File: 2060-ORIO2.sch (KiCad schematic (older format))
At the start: 185 parts, among them J11 RaspberryPI-B+header, J12 Conn_01x04, J13 Conn_01x08, J14 Conn_01x08, J15 Conn_01x08, J16 Conn_01x10, J17 Conn_01x10, J18 Conn_01x10, J19 Conn_01x10, J20 Conn_01x09, J21 Conn_01x08, J22 Conn_01x08, J23 Conn_01x08, J24 Conn_01x08, J25 Conn_01x08, J26 Conn_01x08, J27 Conn_01x02, J28 Conn_01x16, J29 Conn_01x16, J30 Conn_01x16, J31 Conn_01x08, J32 Conn_01x08, J33 Conn_01x08, J34 Conn_01x08, J35 TBL001-500-02GY-2GY, Q11 ULN2803ADWR, SW11 SW_DIP_x08, U11 ICE40HX4K-TQ144, U12 SN74LVC4245AN, U13 SN74LVC4245AN, U14 SN74LVC4245AN, U15 TPS563231, U16 MCP3008, U17 AZ1117CH-3.3TRG1, U18 AZ1117CH-3.3TRG1, U19 AZ1117CH-1.2, U20 TPS563231, U21 SN74LVC4245AN, U22 SN74LVC4245AN, U23 SN74LVC4245AN, U24 SN74LVC4245AN, U25 TPS563231, U26 AP3012, Y11 XLH536025_000000I

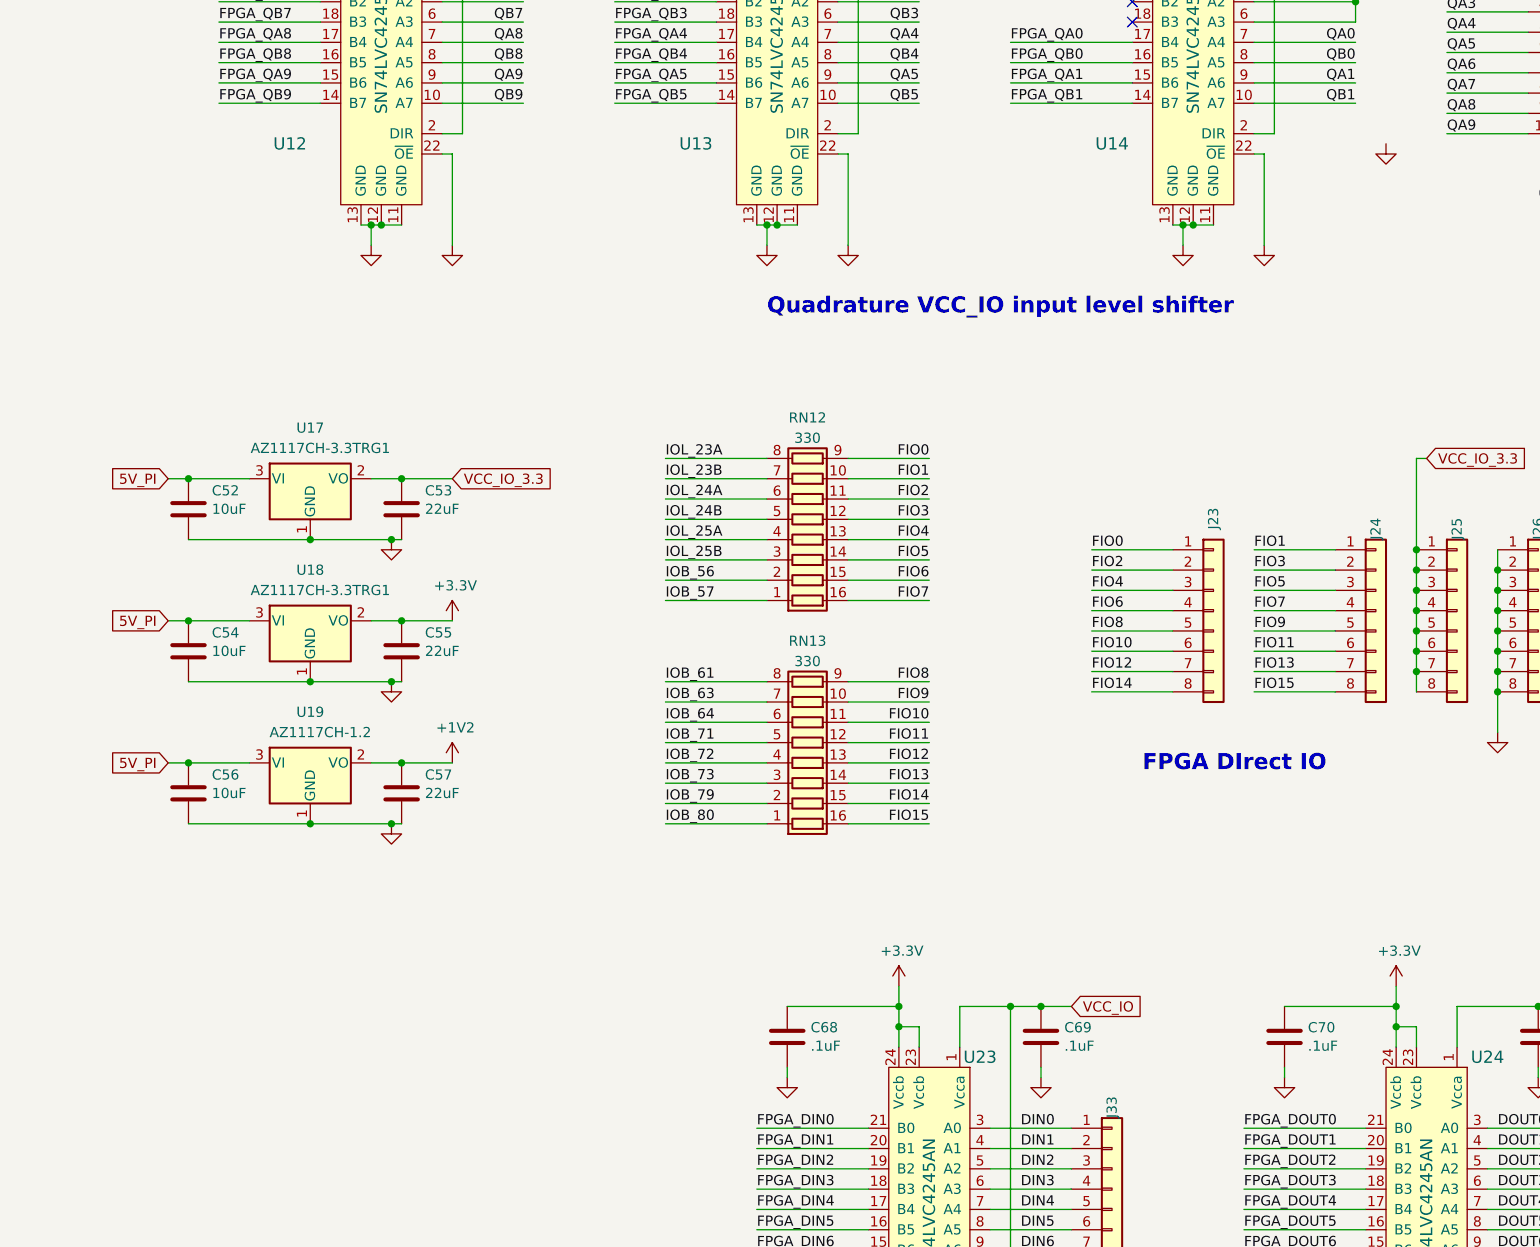
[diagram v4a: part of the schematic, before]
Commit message: Added power LED & GND plane vias.
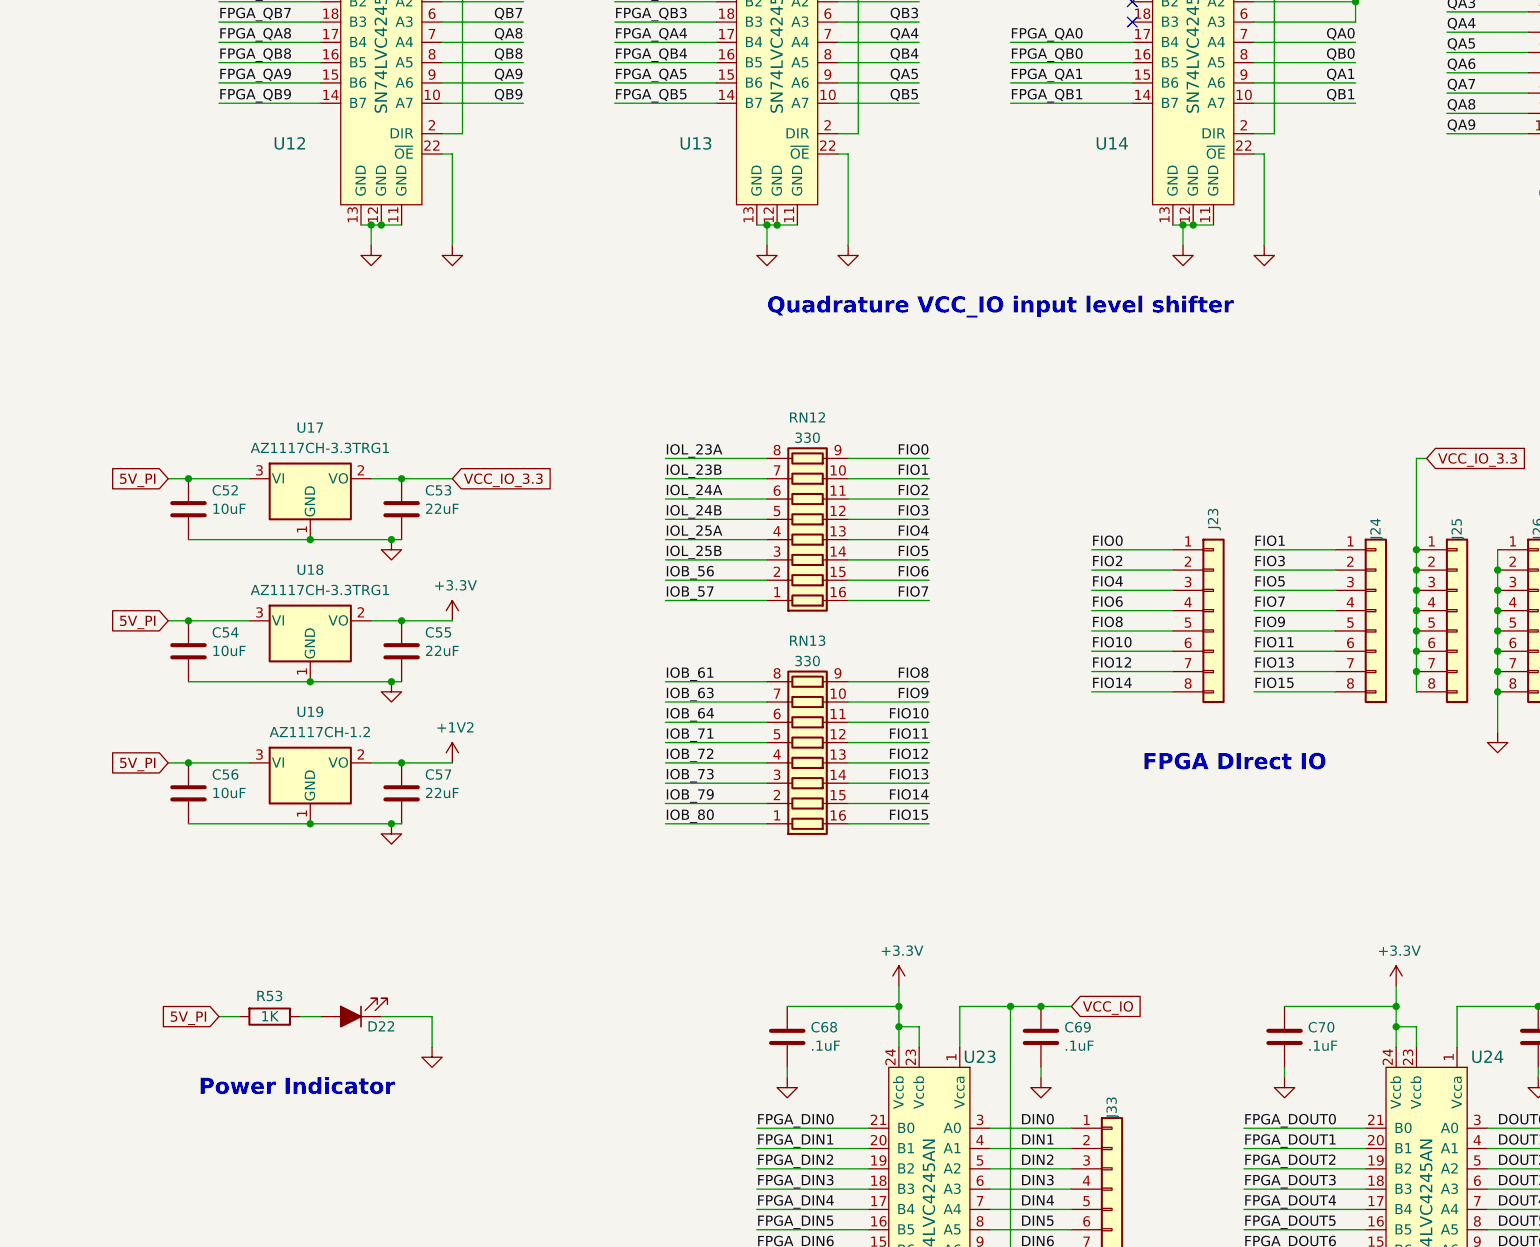
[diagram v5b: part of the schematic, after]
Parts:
- added D22: LED_ALT, LED_SMD:LED_0805_2012Metric_Pad1.15x1.40mm_HandSolder, symbol Device:LED_ALT
- added R53: 1K, Resistor_SMD:R_0603_1608Metric_Pad1.05x0.95mm_HandSolder, symbol Device:R
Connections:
- net 5V_PI: now also R53.2
- net GND: now also D22.1 (K)
- new net: D22.2 (A), R53.1
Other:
- note added: "Power Indicator"
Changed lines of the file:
@@
 	11950 7600 12450 7600
-$Comp
-L power:GND #PWR0121
-U 1 1 5F55C3BD
-P 12600 8200
-F 0 "#PWR0121" H 12600 7950 50  0001 C CNN
-F 1 "GND" H 12605 8027 50  0001 C CNN
-F 2 "" H 12600 8200 50  0001 C CNN
-F 3 "" H 12600 8200 50  0001 C CNN
-	1    12600 8200
-	1    0    0    -1
-$EndComp
 $Comp
 L Device:Net-Tie_2 NT1
@@
 Wire Wire Line
 	12650 7200 12650 7300
+$Comp
+L Device:LED_ALT D22
+U 1 1 5FB53195
+P 7500 12500
+F 0 "D22" H 7350 12550 50  0000 C CNN
+F 1 "LED_ALT" H 7493 12626 50  0001 C CNN
+F 2 "LED_SMD:LED_0805_2012Metric_Pad1.15x1.40mm_HandSolder" H 7500 12500 50  0001 C CNN
+F 3 "~" H 7500 12500 50  0001 C CNN
+F 4 "LED GREEN DIFFUSED 0805 SMD" H 7500 12500 50  0001 C CNN "Description"
+F 5 "475-1410-1-ND" H 7500 12500 50  0001 C CNN "Digi-Key_PN"
+F 6 "LG R971-KN-1" H 7500 12500 50  0001 C CNN "MPN"
+F 7 "OSRAM Opto Semiconductors Inc." H 7500 12500 50  0001 C CNN "Manufacturer"
+	1    7500 12500
+	-1   0    0    1
+$EndComp
+Text GLabel 6850 12500 0    50   Input ~ 0
+5V_PI
+$Comp
+L Device:R R?
+U 1 1 5FB72B9D
+P 7100 12500
+AR Path="/5BBE5CCD/5FB72B9D" Ref="R?"  Part="1"
+AR Path="/5FB72B9D" Ref="R53"  Part="1"
+AR Path="/5CF9559A/5FB72B9D" Ref="R?"  Part="1"
+AR Path="/5ECC13DB/5FB72B9D" Ref="R?"  Part="1"
+F 0 "R53" V 7000 12500 50  0000 C CNN
+F 1 "1K" V 7100 12500 50  0000 C CNN
+F 2 "Resistor_SMD:R_0603_1608Metric_Pad1.05x0.95mm_HandSolder" V 7030 12500 50  0001 C CNN
+F 3 "~" H 7100 12500 50  0001 C CNN
+F 4 "" H 7100 12500 50  0001 C CNN "Digi-Key_PN"
+F 5 "" H 7100 12500 50  0001 C CNN "Description"
+F 6 "" H 7100 12500 50  0001 C CNN "MPN"
+F 7 "Yageo" H 7100 12500 50  0001 C CNN "Manufacturer"
+	1    7100 12500
+	0    1    1    0
+$EndComp
+Wire Wire Line
+	6850 12500 6950 12500
+Wire Wire Line
+	7250 12500 7350 12500
+Wire Wire Line
+	7650 12500 7900 12500
+Wire Wire Line
+	7900 12500 7900 12650
+$Comp
+L power:GND #PWR?
+U 1 1 5FF6D867
+P 7900 12650
+AR Path="/5D1A4D20/5FF6D867" Ref="#PWR?"  Part="1"
+AR Path="/5FF6D867" Ref="#PWR0121"  Part="1"
+AR Path="/5CF9559A/5FF6D867" Ref="#PWR?"  Part="1"
+AR Path="/5E2D04E3/5FF6D867" Ref="#PWR?"  Part="1"
+AR Path="/5F66828B/5FF6D867" Ref="#PWR?"  Part="1"
+F 0 "#PWR0121" H 7900 12400 50  0001 C CNN
+F 1 "GND" H 7905 12477 50  0001 C CNN
+F 2 "" H 7900 12650 50  0001 C CNN
+F 3 "" H 7900 12650 50  0001 C CNN
+	1    7900 12650
+	1    0    0    -1
+$EndComp
+Text Notes 6750 12900 0    79   ~ 16
+Power Indicator
 $EndSCHEMATC

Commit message: Fuses, 4-layer, RSL, 86 the Solenoid GND,
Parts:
- removed J14: Conn_01x08, Connector_PinHeader_2.54mm:PinHeader_1x08_P2.54mm_Vertical, symbol Connector_Generic:Conn_01x08
- added F11: .5A, Fuse:Fuse_2920_7451Metric_Pad2.10x5.45mm_HandSolder, symbol Device:Polyfuse
- added F12: Polyfuse, Fuse:Fuse_2920_7451Metric_Pad2.10x5.45mm_HandSolder, symbol Device:Polyfuse
- added J14: Conn_01x02, Connector_PinHeader_2.54mm:PinHeader_1x02_P2.54mm_Vertical, symbol Connector_Generic:Conn_01x02
- added Q12: BCV27, Package_TO_SOT_SMD:SOT-23, symbol Device:Q_NPN_Darlington_BEC
- added R54: 1K, Resistor_SMD:R_0603_1608Metric_Pad1.05x0.95mm_HandSolder, symbol Device:R
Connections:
- net +BATT: now also F11.2, F12.1; no longer C78.1, D21.1 (K), L14.1, U26.4 (~SHDN), U26.5 (VIN)
- net GND: now also Q12.2 (E)
- net FPGA_RSL: now reaches U11.128 (IOT_197_GBIN1)
- net FPGA_RSL: now also R54.2
- net VCC_SOL renamed VCC_SOL_24
- new net: Q12.1 (B), R54.1
- new net: J14.2 (Pin_2), Q12.3 (C)
- new net: D21.1 (K), F12.2
- new net VCC_SOL_12: C78.1, F11.1, J14.1 (Pin_1), L14.1, U26.4 (~SHDN), U26.5 (VIN)
- no-connect marks 34 -> 33
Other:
- note added: "RSL Light Driver"
- moved on the sheet: C78, C79, D20, J13, L14, R51, R52, U26

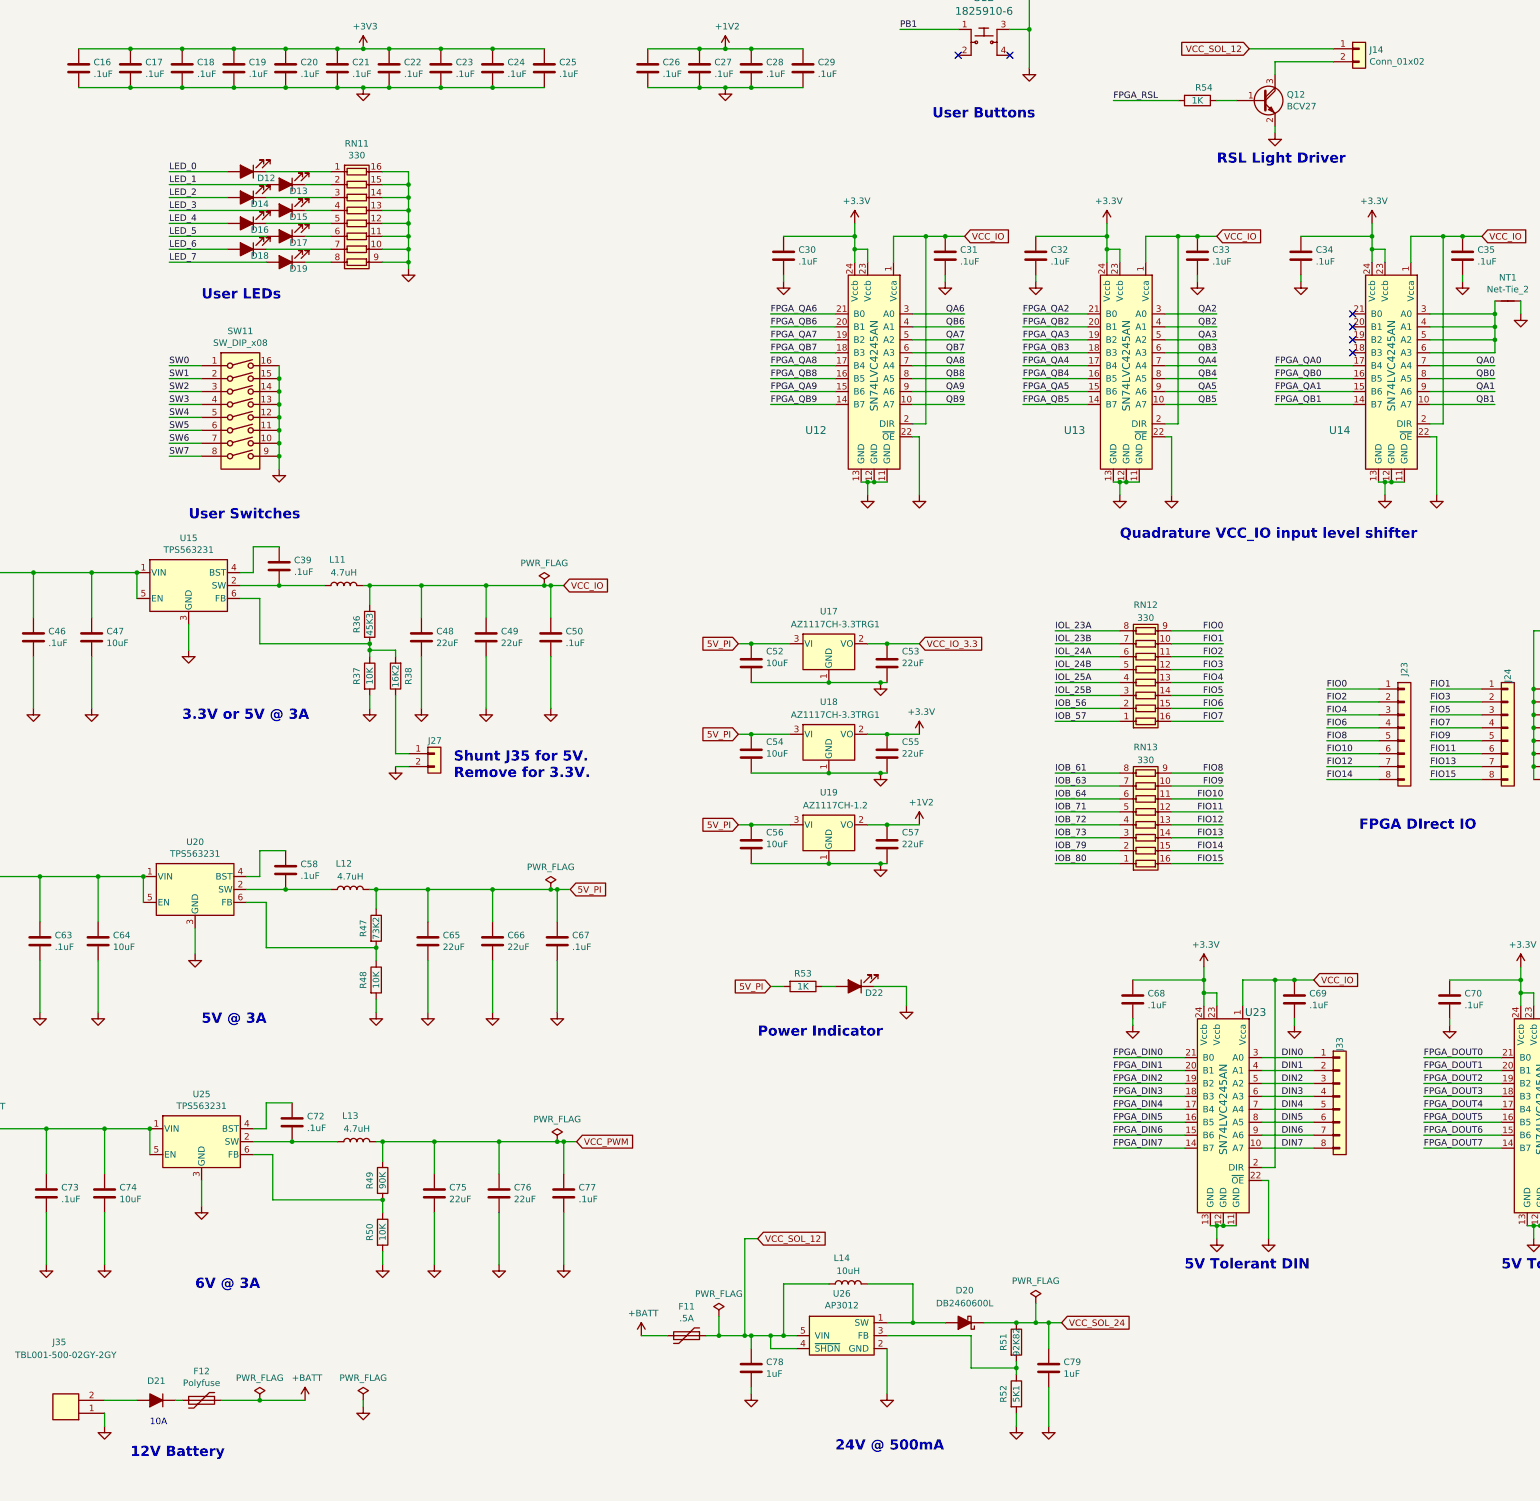
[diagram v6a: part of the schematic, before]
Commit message: Added pul;lup resistors on DIN level shifters.
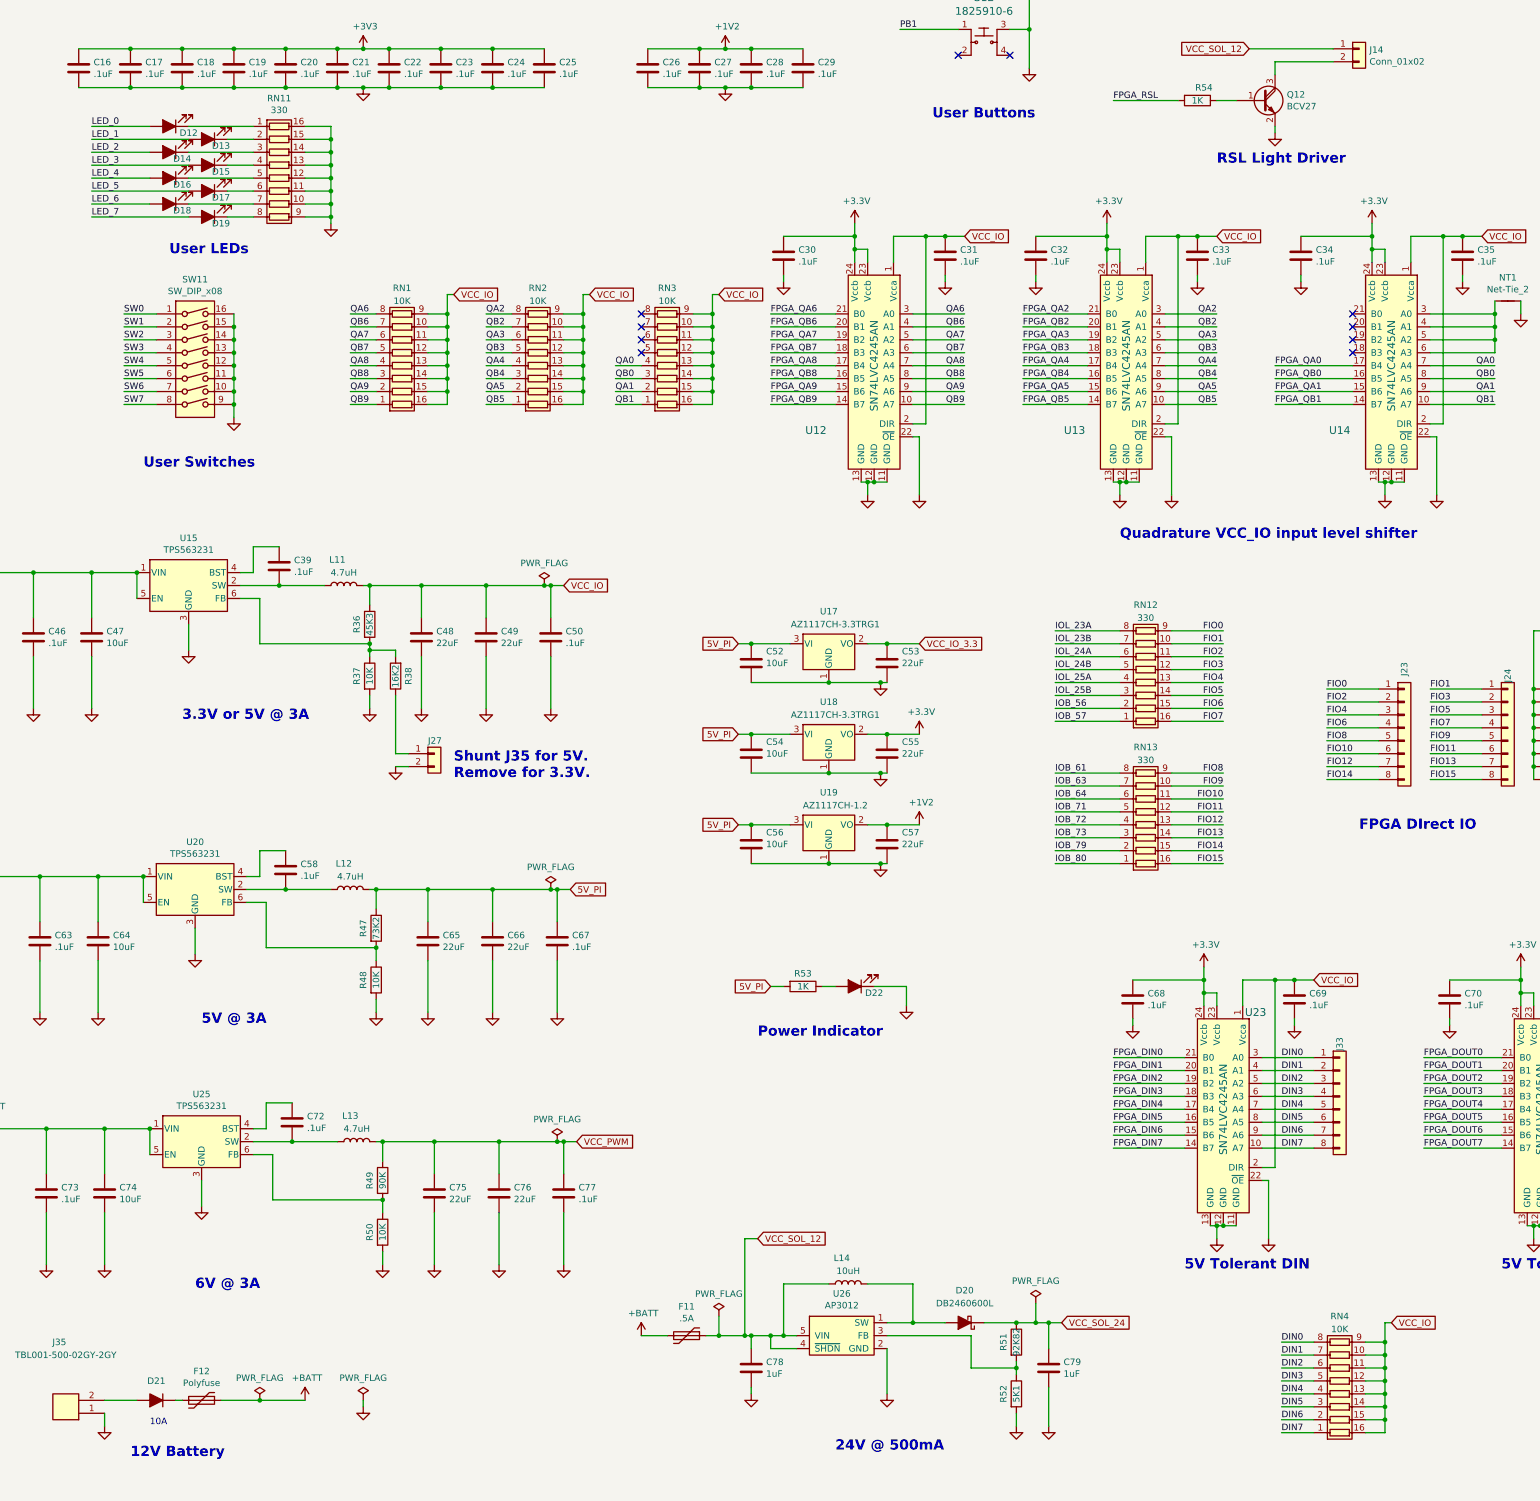
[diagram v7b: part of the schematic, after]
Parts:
- added RN1, RN2, RN3, RN4: 10K, Resistor_SMD:R_Array_Convex_8x0602, symbol Device:R_Pack08
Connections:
- net DIN0: now also RN4.8 (R8.1)
- net DIN1: now also RN4.7 (R7.1)
- net DIN2: now also RN4.6 (R6.1)
- net DIN3: now also RN4.5 (R5.1)
- net DIN4: now also RN4.4 (R4.1)
- net DIN5: now also RN4.3 (R3.1)
- net DIN6: now also RN4.2 (R2.1)
- net DIN7: now also RN4.1 (R1.1)
- net QA0: now also RN3.4 (R4.1)
- net QA1: now also RN3.2 (R2.1)
- net QA2: now also RN2.8 (R8.1)
- net QA3: now also RN2.6 (R6.1)
- net QA4: now also RN2.4 (R4.1)
- net QA5: now also RN2.2 (R2.1)
- net QA6: now also RN1.8 (R8.1)
- net QA7: now also RN1.6 (R6.1)
- net QA8: now also RN1.4 (R4.1)
- net QA9: now also RN1.2 (R2.1)
- net QB0: now also RN3.3 (R3.1)
- net QB1: now also RN3.1 (R1.1)
- net QB2: now also RN2.7 (R7.1)
- net QB3: now also RN2.5 (R5.1)
- net QB4: now also RN2.3 (R3.1)
- net QB5: now also RN2.1 (R1.1)
- net QB6: now also RN1.7 (R7.1)
- net QB7: now also RN1.5 (R5.1)
- net QB8: now also RN1.3 (R3.1)
- net QB9: now also RN1.1 (R1.1)
- net VCC_IO: now also RN1.10 (R7.2), RN1.11 (R6.2), RN1.12 (R5.2), RN1.13 (R4.2), RN1.14 (R3.2), RN1.15 (R2.2), RN1.16 (R1.2), RN1.9 (R8.2), RN2.10 (R7.2), RN2.11 (R6.2), RN2.12 (R5.2), RN2.13 (R4.2), RN2.14 (R3.2), RN2.15 (R2.2), RN2.16 (R1.2), RN2.9 (R8.2), RN3.10 (R7.2), RN3.11 (R6.2), RN3.12 (R5.2), RN3.13 (R4.2), RN3.14 (R3.2), RN3.15 (R2.2), RN3.16 (R1.2), RN3.9 (R8.2), RN4.10 (R7.2), RN4.11 (R6.2), RN4.12 (R5.2), RN4.13 (R4.2), RN4.14 (R3.2), RN4.15 (R2.2), RN4.16 (R1.2), RN4.9 (R8.2)
- no-connect marks 33 -> 37
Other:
- moved on the sheet: D12, D13, D14, D15, D16, D17, D18, D19, RN11, SW11
